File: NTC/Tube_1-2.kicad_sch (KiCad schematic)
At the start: 70 parts, among them Q1 MPSA42, Q10 MPSA42, Q11 MPSA42, Q12 MPSA42, Q13 MPSA42, Q14 MPSA42, Q15 MPSA42, Q16 MPSA42, Q17 MPSA42, Q18 MPSA42, Q19 MPSA42, Q2 MPSA42, Q20 MPSA42, Q21 MPSA42, Q22 MPSA42, Q23 MPSA42, Q24 MPSA42, Q3 MPSA42, Q4 MPSA42, Q5 MPSA42, Q6 MPSA42, Q7 MPSA42, Q8 MPSA42, Q9 MPSA42, X10 Conn_01x06_Socket, X11 Conn_01x04_Socket, X7 Conn_01x06_Socket, X8 Conn_01x06_Socket, X9 Conn_01x06_Socket

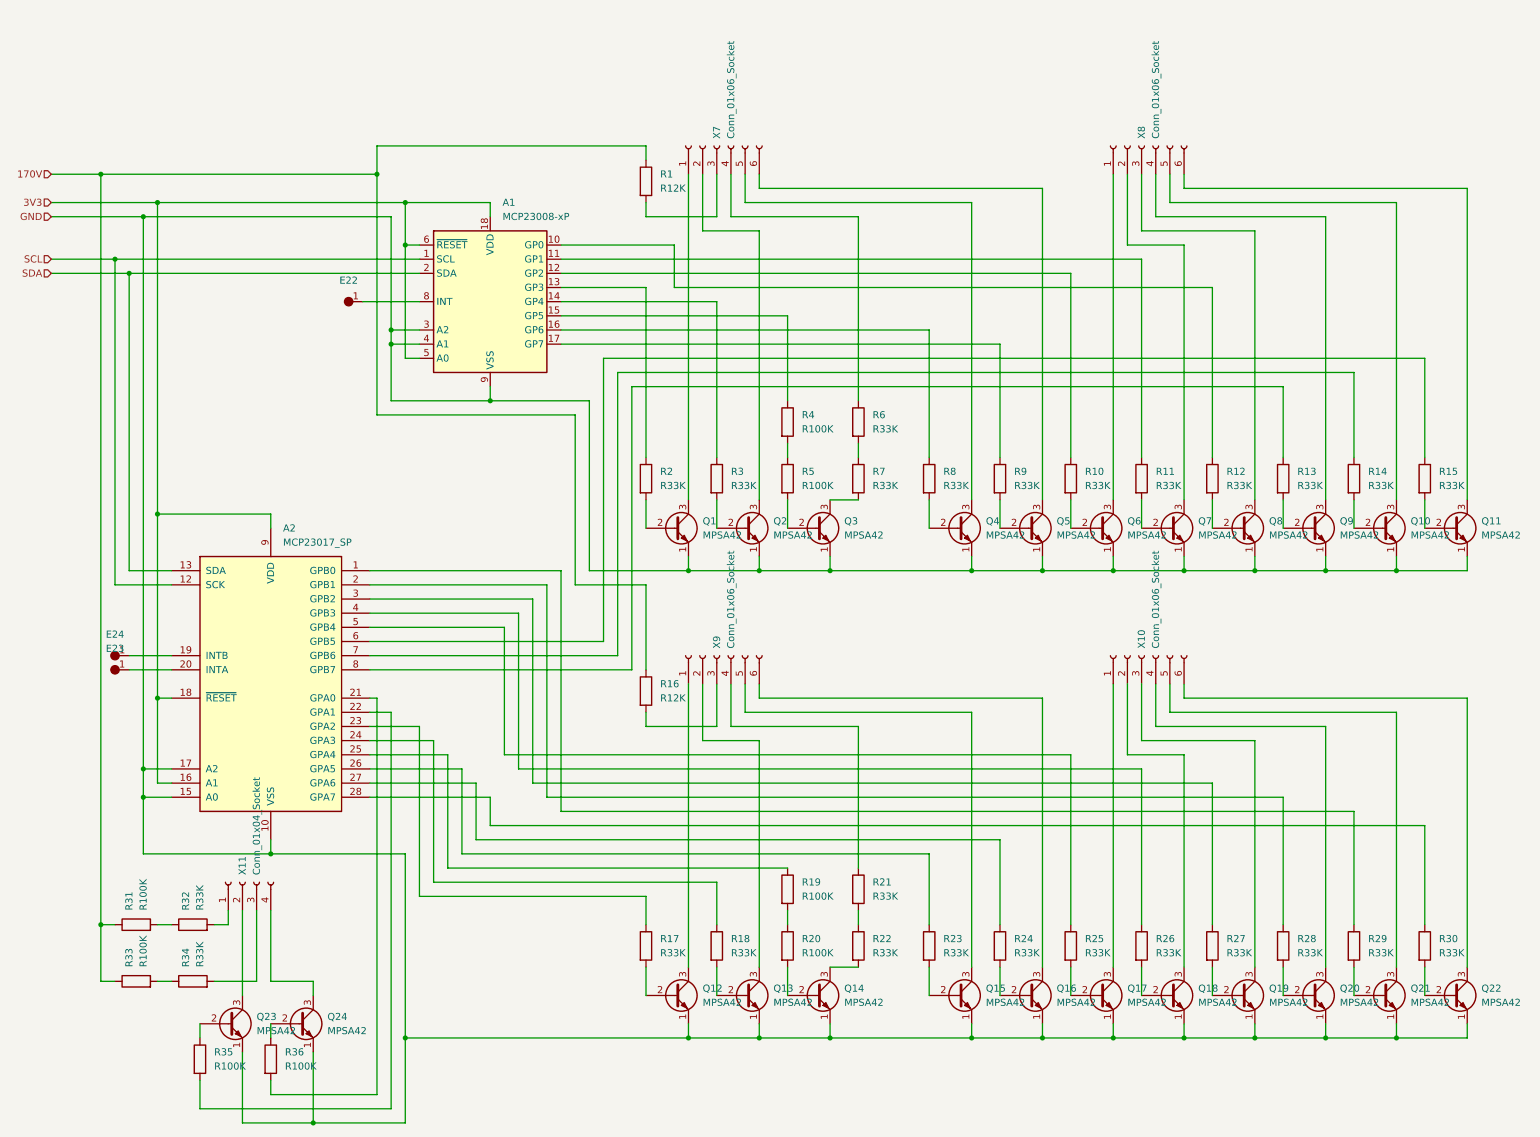
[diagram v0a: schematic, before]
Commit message: Changed to 14pin socket
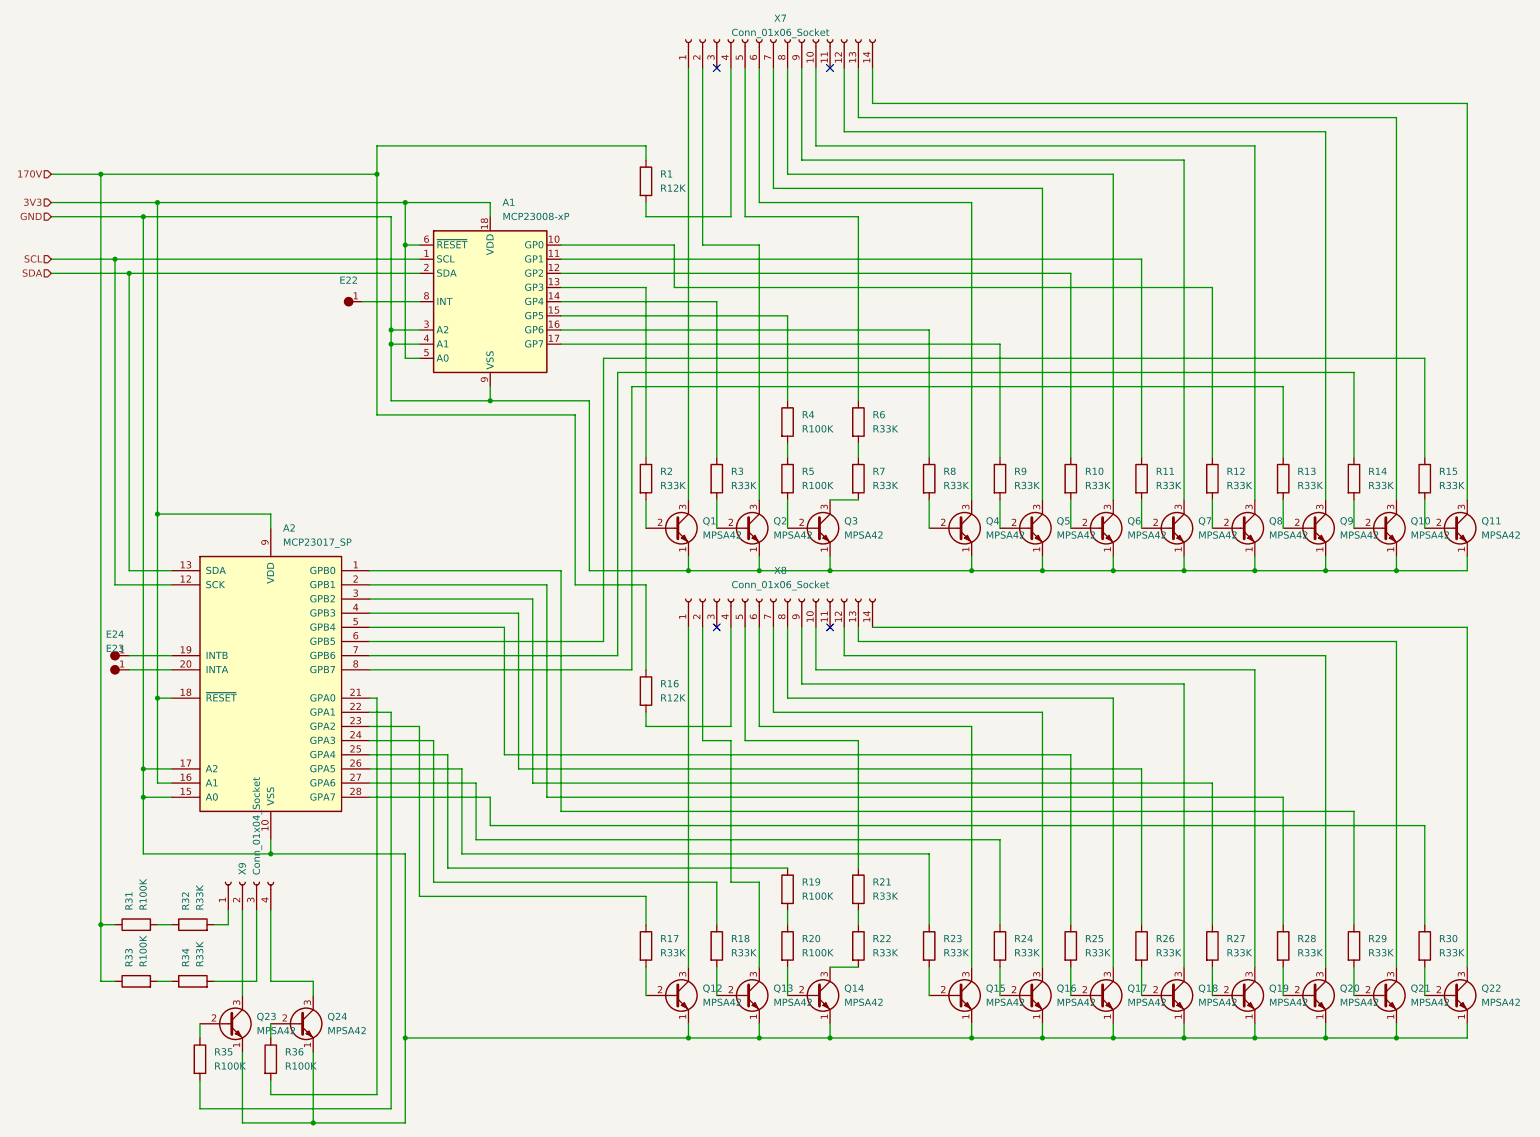
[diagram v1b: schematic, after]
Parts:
- removed X10, X8: Conn_01x06_Socket, Nixie:Pinbar_1-6-f-b, symbol Connector:Conn_01x06_Socket
- A1: footprint Package_DIP:DIP-18_W7.62mm -> Nixie:DIP-18_IC+Socket
- A2: footprint Package_DIP:DIP-28_W7.62mm -> Nixie:DIP-28_IC+Socket
- Q1, Q10, Q11, Q12, Q13, Q14, Q15, Q16, Q17, Q18, Q19, Q2, Q20, Q21, Q22, Q23, Q24, Q3, Q4, Q5, Q6, Q7, Q8, Q9: footprint Package_TO_SOT_THT:TO-92_Inline -> Nixie:MPSA-42
- X7: footprint Nixie:Pinbar_1-6-f-a -> Nixie:Pinbar_4-14-f; symbol Connector:Conn_01x06_Socket -> Connector:Conn_01x14_Socket
- X8: renamed from X9; footprint Nixie:Pinbar_1-6-f-a -> Nixie:Pinbar_4-14-f; symbol Connector:Conn_01x06_Socket -> Connector:Conn_01x14_Socket
- renumbered X11 to X9
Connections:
- net at X7.3 (Pin_3): no longer R1.2
- net at X7.4 (Pin_4): now also R1.2; no longer R6.1
- net at X7.5 (Pin_5): now also R6.1; no longer Q4.3 (C)
- net at X7.6 (Pin_6): now also Q4.3 (C); no longer Q5.3 (C)
- net at R16.2: now also X8.4 (Pin_4); no longer X8.3 (Pin_3)
- net at Q19.3 (C): now also X8.10 (Pin_10)
- net at Q7.3 (C): now also X7.9 (Pin_9)
- net at Q6.3 (C): now also X7.8 (Pin_8)
- net at Q8.3 (C): now also X7.10 (Pin_10)
- net at Q9.3 (C): now also X7.12 (Pin_12)
- net at Q10.3 (C): now also X7.13 (Pin_13)
- net at Q11.3 (C): now also X7.14 (Pin_14)
- net at Q21.3 (C): now also X8.13 (Pin_13)
- net at Q22.3 (C): now also X8.14 (Pin_14)
- net at Q20.3 (C): now also X8.12 (Pin_12)
- net at R21.1: now also X8.5 (Pin_5); no longer X8.4 (Pin_4)
- net at Q17.3 (C): now also X8.8 (Pin_8)
- net at Q15.3 (C): now also X8.6 (Pin_6); no longer X8.5 (Pin_5)
- net at Q16.3 (C): now also X8.7 (Pin_7); no longer X8.6 (Pin_6)
- net at Q18.3 (C): now also X8.9 (Pin_9)
- new net: Q5.3 (C), X7.7 (Pin_7)
- no-connect marks 0 -> 4

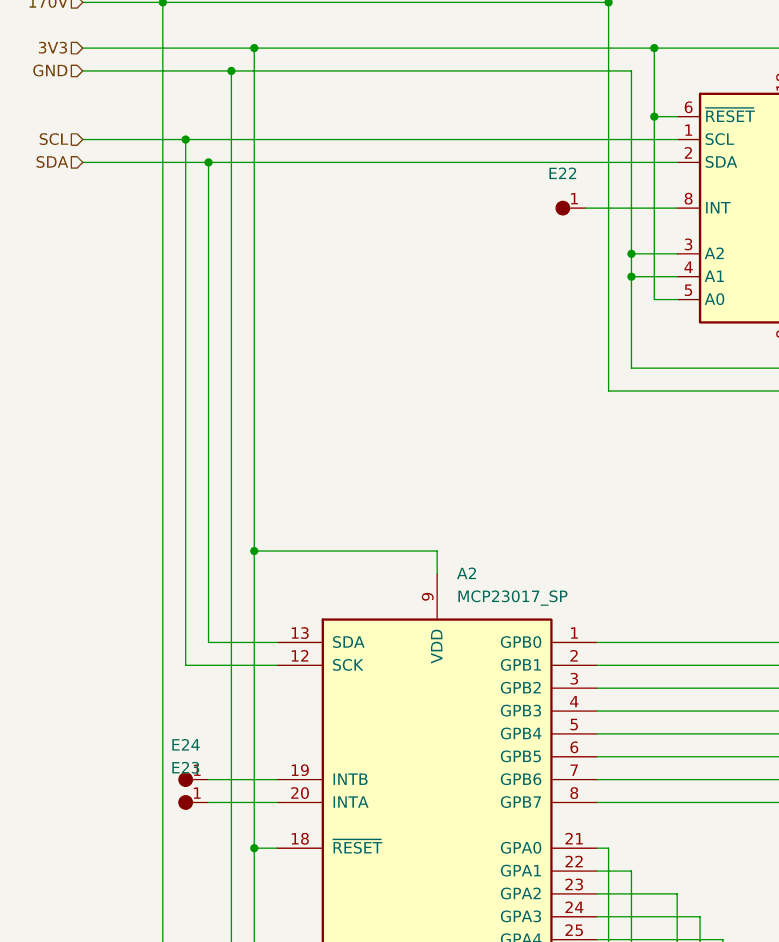
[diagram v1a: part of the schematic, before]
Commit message: Added GPS
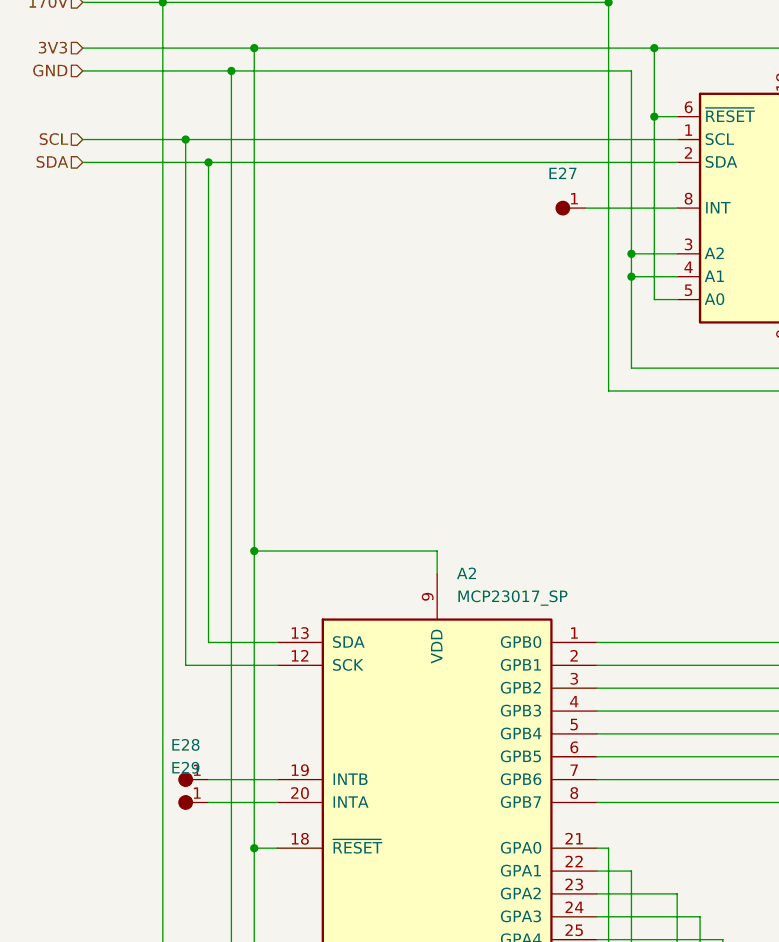
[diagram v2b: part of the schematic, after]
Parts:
- renumbered E22 to E27, E24 to E28, E23 to E29
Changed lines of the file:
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@@
 		(dnp no)
 		(fields_autoplaced yes)
-		(property "Reference" "E24"
+		(property "Reference" "E28"
 			(at 30.48 106.68 0)
 			(effects
@@
 			(project ""
 				(path "/ecf22f8e-0676-4495-9357-338c1fd23f92/e5fbc528-9efe-46d3-8950-ffadc99b624b"
-					(reference "E24")
+					(reference "E28")
 					(unit 1)
 				)
@@
 		(dnp no)
 		(fields_autoplaced yes)
-		(property "Reference" "E23"
+		(property "Reference" "E29"
 			(at 30.48 109.22 0)
 			(effects
@@
 			(project ""
 				(path "/ecf22f8e-0676-4495-9357-338c1fd23f92/e5fbc528-9efe-46d3-8950-ffadc99b624b"
-					(reference "E23")
+					(reference "E29")
 					(unit 1)
 				)
@@
 		(dnp no)
 		(fields_autoplaced yes)
-		(property "Reference" "E22"
+		(property "Reference" "E27"
 			(at 72.39 43.18 0)
 			(effects
@@
 			(project ""
 				(path "/ecf22f8e-0676-4495-9357-338c1fd23f92/e5fbc528-9efe-46d3-8950-ffadc99b624b"
-					(reference "E22")
-					(unit 1)
-				)
+					(reference "E27")
+					(unit 1)
+				)
